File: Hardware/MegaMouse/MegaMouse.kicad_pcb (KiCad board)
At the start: 2 copper layers, 93.1 x 193 mm, 71 parts, among them J101 SHIFT_CONN, J102 PROG_CONN, J103 SHIFT_CONN, J104 PROG_CONN, J201 Motor, J301 Motor, J401 ICSP, J601 USBC, SW401 RESET, SW402 START_SW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

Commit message: Bump all
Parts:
- added G***: LOGO, KenwoodFox:KITSUNE_LOGO, F.Cu at (-29.0, 82.0)
- added REF**: OSHW-Logo2_14.6x12mm_SilkScreen, Symbol:OSHW-Logo2_14.6x12mm_SilkScreen, F.Cu at (29.2, 82.5)
- moved R602 205.7 mm to (8.60, 100.5), turned to 90 degrees
- moved D601 204.7 mm to (-7.20, 98.1), turned to -90 degrees
- moved R601 202.9 mm to (6.60, 100.5), turned to 90 degrees
- moved C603 192.0 mm to (17.2, 85.1), turned to -90 degrees
- moved C604 191.4 mm to (17.2, 81.5), turned to 90 degrees
- moved C602 191.1 mm to (4.75, 83.6), turned to 180 degrees
- moved R606 190.8 mm to (10.3, 88.8), turned to 90 degrees
- moved R605 188.9 mm to (12.3, 88.8), turned to 90 degrees
- moved R603 186.3 mm to (4.70, 79.5), turned to 180 degrees
- moved C601 186.0 mm to (4.70, 77.5), turned to 180 degrees
- moved J601 185.5 mm to (0.10, 100.5), turned to 0 degrees
- moved R604 182.8 mm to (3.55, 81.5)
- moved H604 178.4 mm to (16.1, 95.5), turned to 180 degrees
- moved H602 178.4 mm to (-15.9, 95.5), turned to 180 degrees
- moved D602 177.3 mm to (-6.56, 74.0), turned to 180 degrees
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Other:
- board size 93.1 x 193 mm -> 93.1 x 158.2 mm

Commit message: Even more stuff! also bump libs
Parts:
- added G***: LOGO, KenwoodFox:KITSUNE_LOGO, B.Cu at (-38.4, 45.0)
- added R101: 1K, Resistor_SMD:R_0805_2012Metric, F.Cu at (-41.7, 49.0)
- added R102: 1K, Resistor_SMD:R_0805_2012Metric, F.Cu at (-43.8, 49.0)
- added R103: 1K, Resistor_SMD:R_0805_2012Metric, F.Cu at (44.3, 49.1)
- added R104: 1K, Resistor_SMD:R_0805_2012Metric, F.Cu at (41.8, 49.1)
- added R201: 15k, Resistor_SMD:R_0805_2012Metric, F.Cu at (-33.1, -22.8)
- added R301: 15k, Resistor_SMD:R_0805_2012Metric, F.Cu at (24.0, -22.2)
- added REF**: ESD-Logo_8.9x8mm_SilkScreen, Symbol:ESD-Logo_8.9x8mm_SilkScreen, F.Cu at (-14.6, 76.9)
- added REF**: ESD-Logo_8.9x8mm_SilkScreen, Symbol:ESD-Logo_8.9x8mm_SilkScreen, B.Cu at (-3.50, 3.30)
- added REF**: OSHW-Logo_19x20mm_SilkScreen, Symbol:OSHW-Logo_19x20mm_SilkScreen, B.Cu at (0.00, -42.4)
- added REF**: KiCad-Logo2_20mm_SilkScreen, Symbol:KiCad-Logo2_20mm_SilkScreen, B.Cu at (-0.68, 50.3)
- added SW501: PWR, KenwoodFox:EG1218, F.Cu at (43.1, 31.5)
- moved BT502 72.0 mm to (36.0, 55.0), turned to 180 degrees
- moved U401 2.00 mm to (0.00, -18.0)
- moved C301 1.64 mm to (24.5, -26.9)
- moved C201 1.20 mm to (-24.3, -26.0)
- moved U301 0.40 mm to (28.5, -19.5), turned to -90 degrees
- turned U201 to -90 degrees
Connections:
- BT501 pad 1: +BATT -> Net-(BT501-Pad1)
- C201 pad 1: +5V -> +BATT
- C301 pad 1: +5V -> +BATT
- D101 pad 1: unconnected-(D101-Pad1) -> Net-(D101-Pad1)
- D101 pad 2: unconnected-(D101-Pad2) -> Net-(D101-Pad2)
- D101 pad 3: unconnected-(D101-Pad3) -> GND
- D102 pad 1: unconnected-(D102-Pad1) -> Net-(D102-Pad1)
- D102 pad 2: unconnected-(D102-Pad2) -> Net-(D102-Pad2)
- D102 pad 3: unconnected-(D102-Pad3) -> GND
- J201 pad 3: unconnected-(J201-Pad3) -> /LeftMotor/EncA
- J201 pad 4: unconnected-(J201-Pad4) -> /LeftMotor/EncB
- J301 pad 3: unconnected-(J301-Pad3) -> /RightMotor/EncA
- J301 pad 4: unconnected-(J301-Pad4) -> /RightMotor/EncB
- U201 pad 2: unconnected-(U201-Pad2) -> /LeftMotor/IN2
- U201 pad 3: unconnected-(U201-Pad3) -> /LeftMotor/IN1
- U201 pad 4: unconnected-(U201-Pad4) -> Net-(U201-Pad4)
- U201 pad 5: +5V -> +BATT
- U301 pad 2: unconnected-(U301-Pad2) -> /RightMotor/IN2
- U301 pad 3: unconnected-(U301-Pad3) -> /RightMotor/IN1
- U301 pad 4: unconnected-(U301-Pad4) -> Net-(U301-Pad4)
- U301 pad 5: +5V -> +BATT
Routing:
- net Net-(BT501-Pad2): track 0.00 -> 75.6 mm

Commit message: Add silk
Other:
- board text added: "MegaMouse ${FULL_REVISION}"
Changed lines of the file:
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@@
   (gr_arc (start 46.5 65.5) (mid 46.207107 66.207107) (end 45.5 66.5) (layer "Edge.Cuts") (width 0.1))
   (gr_arc (start 0.1 104.25) (mid -27.781729 96.061488) (end -46.4 73.75) (layer "Edge.Cuts") (width 0.1))
+  (gr_text "MegaMouse\n${FULL_REVISION}" (at 0 28.8) (layer "B.SilkS")
+    (effects (font (size 3 3) (thickness 0.7)) (justify mirror))
+  )
   (gr_text "Maze Cell" (at -69.5 -82) (layer "Cmts.User")
     (effects (font (size 3 3) (thickness 0.15)))

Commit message: Awesomeness
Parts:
- removed C502: 100nF, Capacitor_SMD:C_0805_2012Metric
- removed SW403: STOP/MODE_SW, Button_Switch_THT:SW_PUSH_6mm_H5mm
- C403, C404: footprint Capacitor_SMD:C_0805_2012Metric -> Capacitor_SMD:C_0201_0603Metric
- SW402: value START_SW -> START/MODE; footprint Button_Switch_THT:SW_PUSH_6mm_H5mm -> Button_Switch_THT:SW_Tactile_SKHH_Angled
- moved SW402 177.0 mm to (-43.5, 31.5), turned to 90 degrees
- moved SW401 126.9 mm to (-3.25, 16.9)
- moved Y401 105.9 mm to (-7.80, -18.7), turned to -45 degrees
- moved C504 105.1 mm to (14.8, 21.5), turned to 180 degrees
- moved C403 103.4 mm to (-4.69, -20.8), turned to -45 degrees
- moved C404 99.9 mm to (-5.74, -21.9), turned to 135 degrees
- moved U501 88.3 mm to (23.9, 19.4), turned to 180 degrees
- moved R501 85.8 mm to (40.8, 40.1), turned to -90 degrees
- moved C503 76.8 mm to (17.6, 20.8), turned to 90 degrees
- moved C501 75.7 mm to (31.1, 19.5), turned to -90 degrees
- moved D501 68.9 mm to (43.1, 40.2), turned to -90 degrees
- moved U401 12.0 mm to (0.00, -30.0)
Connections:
- J103 pad 2: unconnected-(J103-Pad2) -> /MCU/DATA_OUT
- J103 pad 3: unconnected-(J103-Pad3) -> /MCU/LATCH_OUT
- J103 pad 4: unconnected-(J103-Pad4) -> /MCU/CLOCK_OUT
- R405 pad 1: /MCU/START -> /MCU/START/MODE
- SW402 pad 1: /MCU/START -> /MCU/START/MODE
- U401 pad 12: /MCU/STOP/MODE -> /MCU/START/MODE
- U401 pad 13: /MCU/START -> /MCU/DATA_OUT
- U401 pad 14: unconnected-(U401-Pad14) -> /MCU/LATCH_OUT
- U401 pad 32: unconnected-(U401-Pad32) -> /MCU/CLOCK_OUT
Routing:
- net +5V: track 0.00 -> 57.5 mm, vias 0 -> 1
- net Net-(C403-Pad1): track 0.00 -> 12.5 mm
- net Net-(C404-Pad1): track 0.00 -> 12.4 mm
- net GND: track 0.00 -> 2.18 mm, vias 0 -> 3
- added copper zone on F.Cu, net +5V

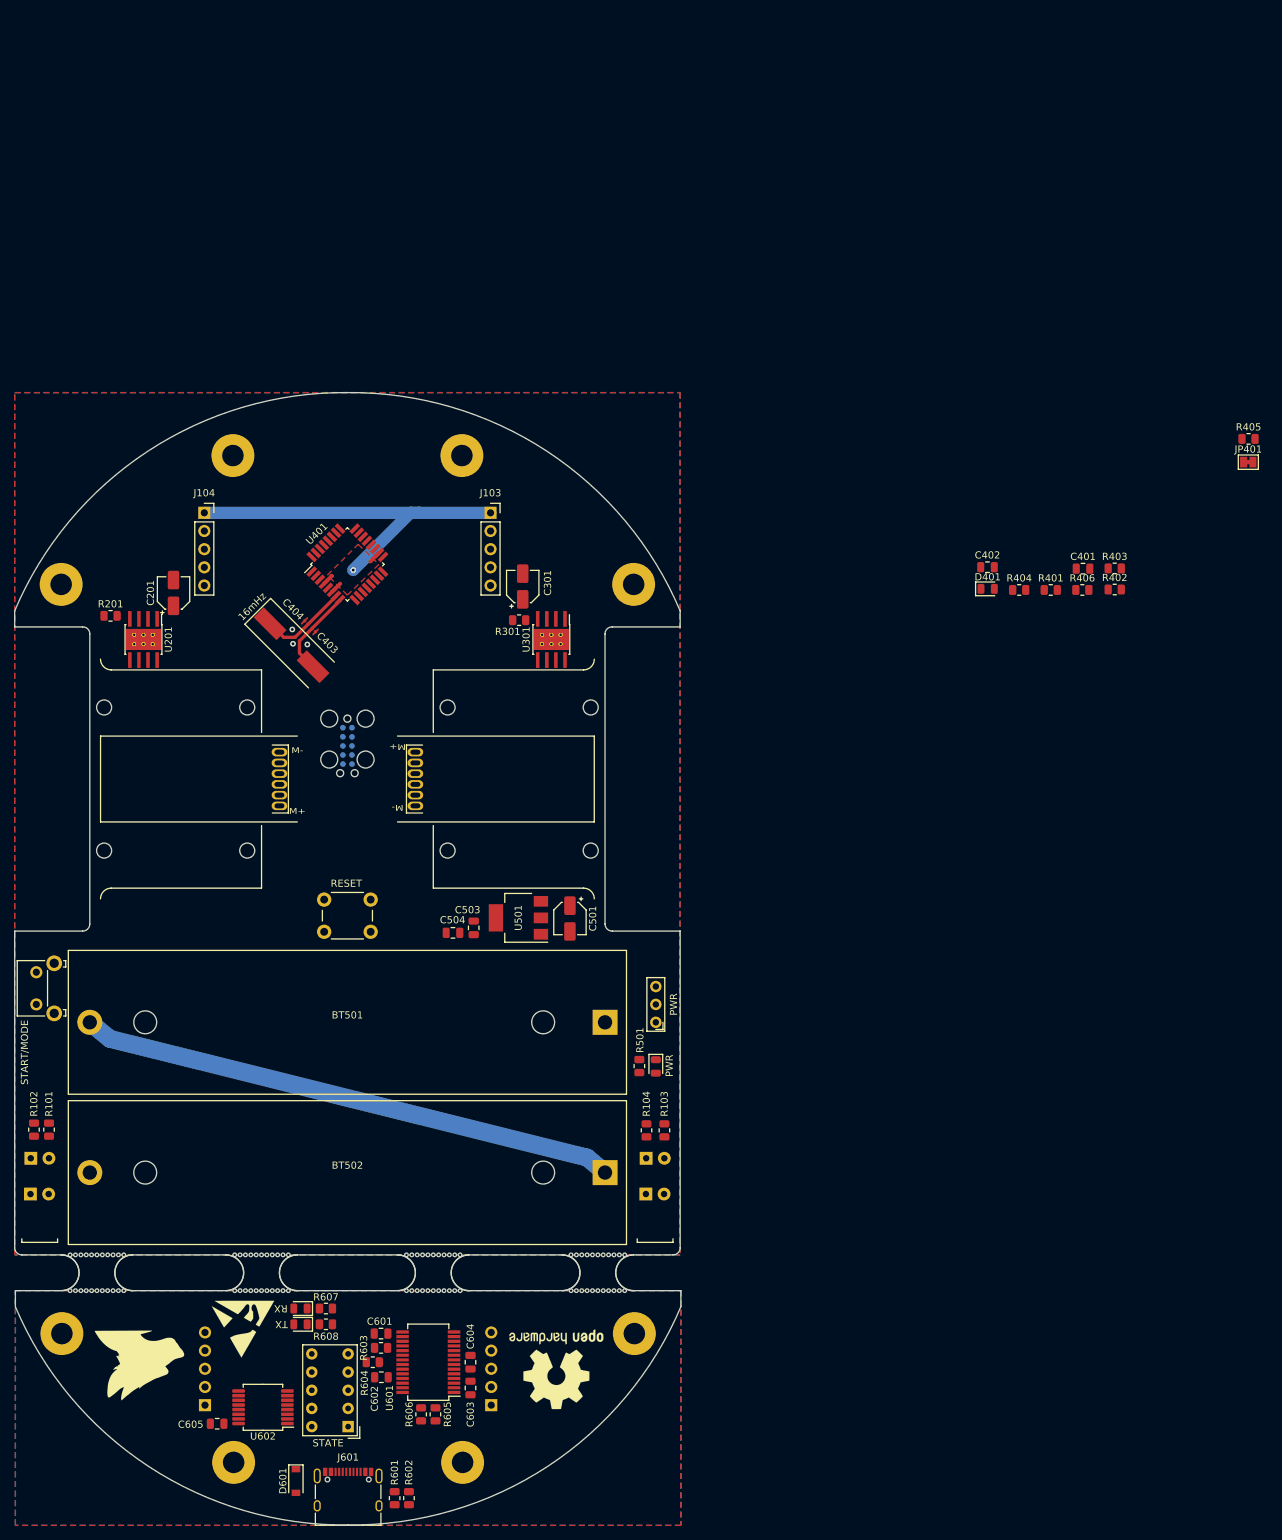
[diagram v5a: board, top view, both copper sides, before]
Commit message: Add decoupling caps and 3d models
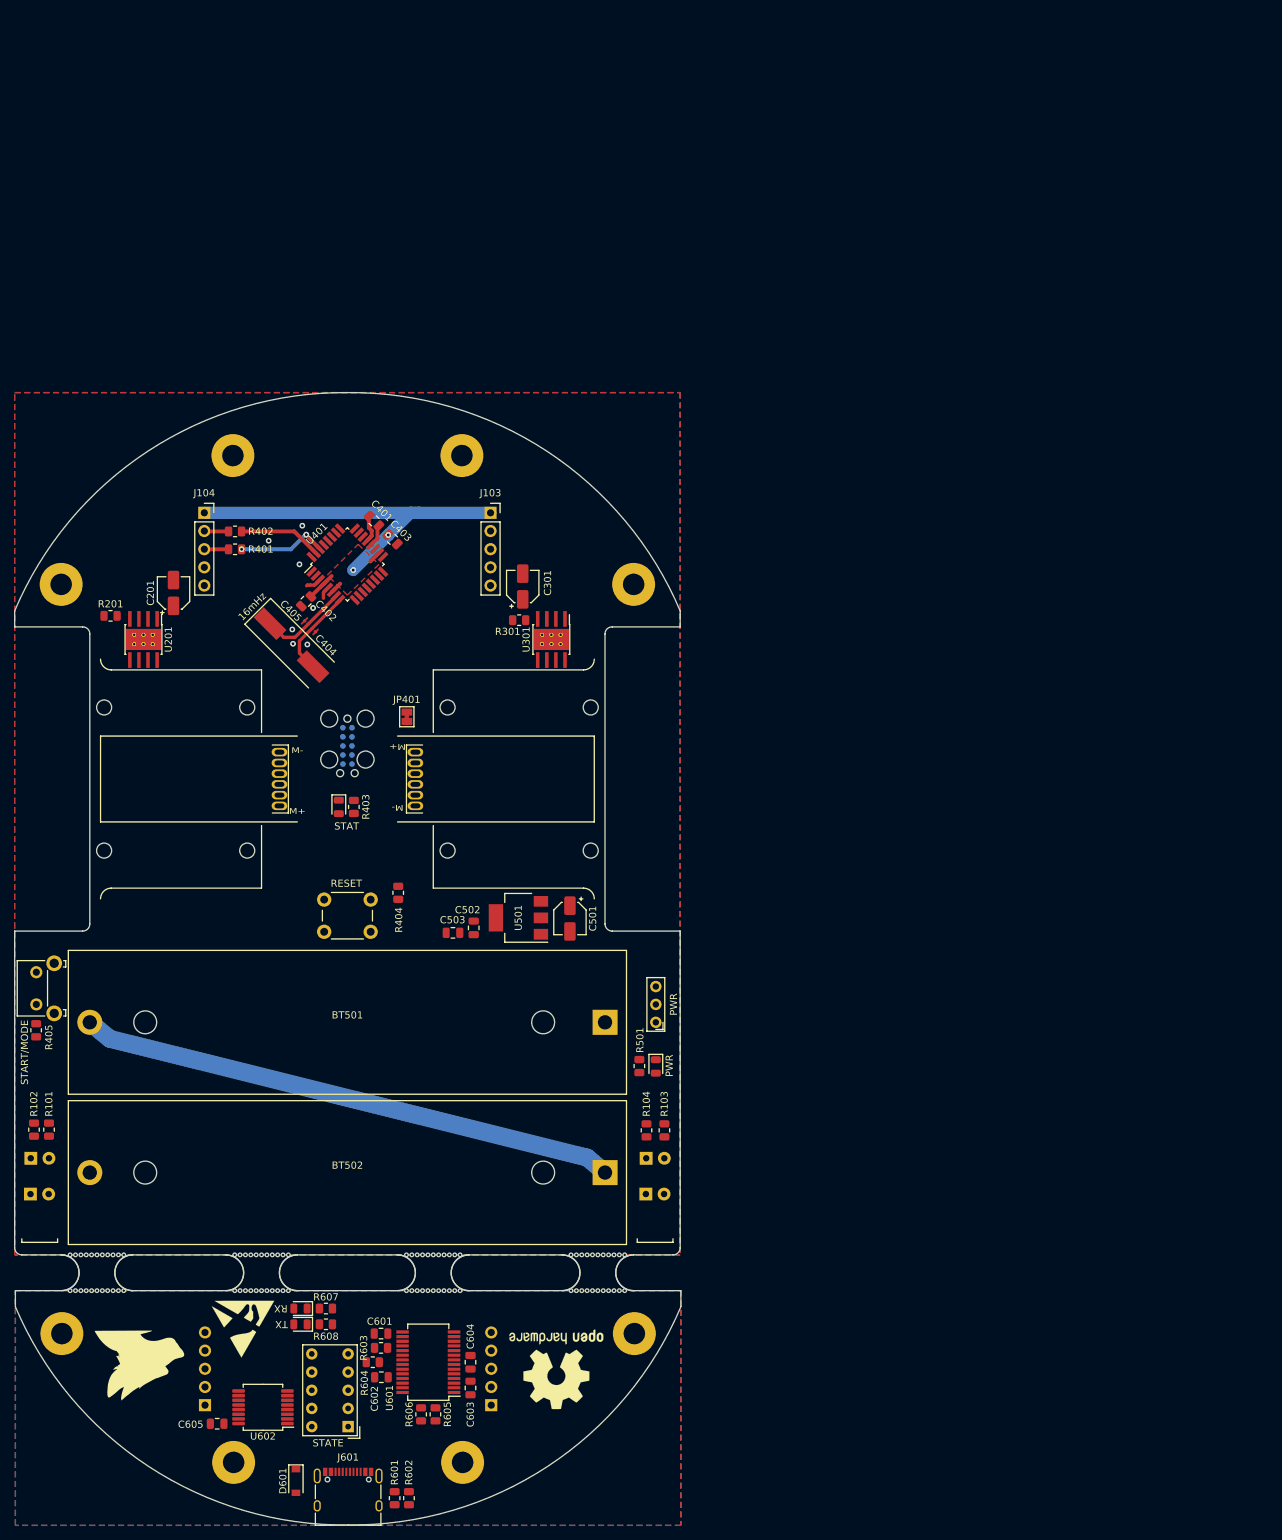
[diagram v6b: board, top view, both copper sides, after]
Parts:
- removed R406: 10K, Resistor_SMD:R_0805_2012Metric
- added C402: 100nF, Capacitor_SMD:C_0805_2012Metric, F.Cu at (-5.77, -24.8)
- moved R405 188.5 mm to (-43.5, 35.1), turned to -90 degrees
- moved R402 123.2 mm to (-15.7, -34.6), turned to 180 degrees
- moved JP401 122.9 mm to (8.30, -8.70), turned to -90 degrees
- moved R401 114.1 mm to (-15.7, -32.1), turned to 180 degrees
- moved R403 111.4 mm to (0.90, 3.90), turned to 90 degrees
- moved C401 99.3 mm to (3.73, -36.1), turned to 135 degrees
- moved R404 96.5 mm to (7.10, 15.9), turned to -90 degrees
- moved D401 95.7 mm to (-1.20, 3.90), turned to -90 degrees
- moved C403 83.2 mm to (6.30, -33.5), turned to -45 degrees
- renumbered C402 to C403, C403 to C404, C404 to C405, C503 to C502, C504 to C503
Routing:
- net Net-(R401-Pad1): track 0.00 -> 12.7 mm, vias 0 -> 2
- net Net-(R402-Pad1): track 0.00 -> 11.6 mm
- net GND: track 2.18 -> 10.0 mm, vias 3 -> 7
- net /MCU/TXD: track 0.00 -> 3.41 mm
- net /MCU/RXD: track 0.00 -> 3.40 mm
- net Net-(C401-Pad1): track 0.00 -> 3.16 mm
- net +5V: track 57.5 -> 60.1 mm, vias 1 -> 2

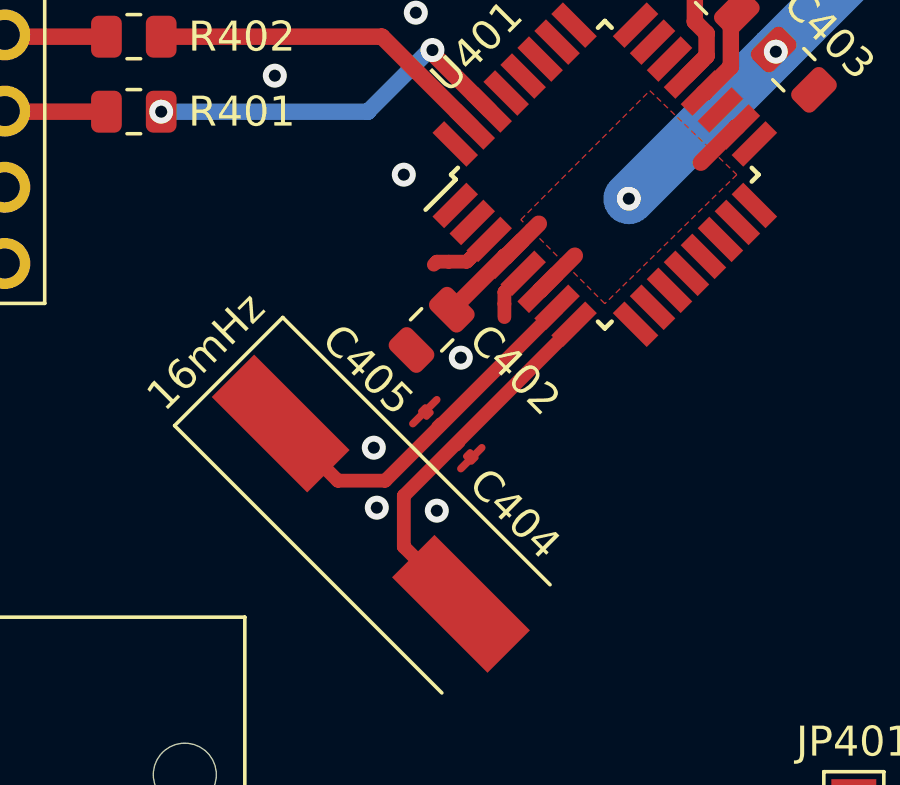
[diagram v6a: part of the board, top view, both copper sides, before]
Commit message: Fix crystal
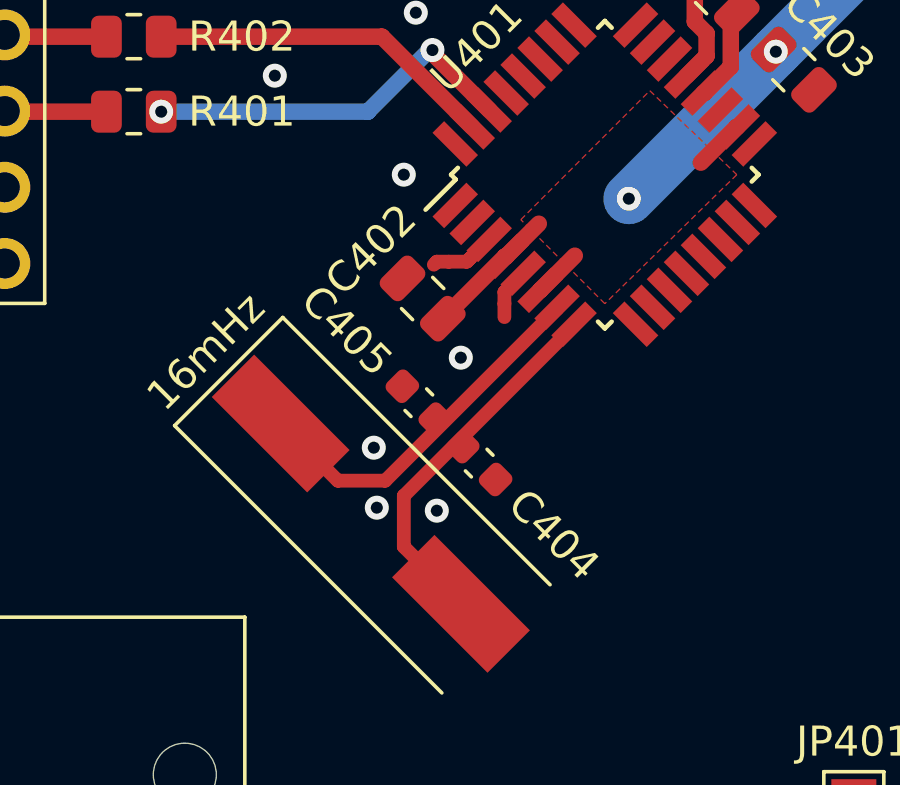
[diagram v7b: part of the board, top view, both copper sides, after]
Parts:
- C404, C405: footprint Capacitor_SMD:C_0201_0603Metric -> Capacitor_SMD:C_0603_1608Metric
- moved C402 1.09 mm to (-6.07, -25.9), turned to 135 degrees
- moved C405 0.71 mm to (-6.20, -22.4)
- moved C404 0.67 mm to (-4.19, -20.4)
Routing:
- net GND: track 10.0 -> 7.83 mm

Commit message: Add more wiring
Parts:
- added TP401: TestPoint, TestPoint:TestPoint_Pad_2.0x2.0mm, B.Cu at (1.60, -12.1)
- added TP402: TestPoint, TestPoint:TestPoint_Pad_2.0x2.0mm, B.Cu at (4.80, -13.5)
- added TP403: TestPoint, TestPoint:TestPoint_Pad_2.0x2.0mm, B.Cu at (-1.60, -12.1)
- added TP404: TestPoint, TestPoint:TestPoint_Pad_2.0x2.0mm, B.Cu at (7.90, -15.0)
- moved C201 9.18 mm to (-31.5, -20.3)
- moved C301 8.52 mm to (22.2, -18.7), turned to 180 degrees
- moved R201 5.77 mm to (-28.0, -25.5), turned to -90 degrees
- moved REF** 3.50 mm to (0.00, 3.20)
- moved U201 2.30 mm to (-26.2, -19.5)
- moved C403 2.19 mm to (7.90, -35.0)
- moved C503 1.15 mm to (15.9, 21.5), turned to 90 degrees
- moved C502 0.78 mm to (18.0, 21.5)
- moved R301 0.73 mm to (23.8, -22.9)
- moved JP401 0.40 mm to (7.90, -8.70)
- turned J401 to 0 degrees
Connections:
- J201 pad 1: /LeftMotor/M1 -> /LeftMotor/M2
- J201 pad 6: /LeftMotor/M2 -> /LeftMotor/M1
- J301 pad 1: /RightMotor/M1 -> /RightMotor/M2
- J301 pad 6: /RightMotor/M2 -> /RightMotor/M1
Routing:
- net +BATT: track 0.00 -> 183.7 mm, vias 0 -> 3
- net +5V: track 60.1 -> 166.1 mm, vias 2 -> 5
- net /MCU/RST: track 0.00 -> 46.9 mm, vias 0 -> 3
- net /MCU/SCK: track 0.00 -> 39.8 mm, vias 0 -> 3
- net /RightMotor/M2: track 0.00 -> 32.5 mm
- net /MCU/SDI: track 0.00 -> 32.2 mm, vias 0 -> 3
- net /LeftMotor/M1: track 0.00 -> 29.6 mm
- net /RightMotor/M1: track 0.00 -> 27.4 mm
- net /MCU/SDO: track 0.00 -> 27.2 mm, vias 0 -> 3
- net /LeftMotor/M2: track 0.00 -> 24.5 mm
- net /MCU/ICSP_RST: track 0.00 -> 7.59 mm, vias 0 -> 1
- net Net-(BT501-Pad1): track 0.00 -> 7.10 mm
- net Net-(R201-Pad2): track 0.00 -> 2.26 mm
- net GND: track 7.83 -> 10.1 mm, vias 7 -> 33
- net Net-(R301-Pad2): track 0.00 -> 2.10 mm
